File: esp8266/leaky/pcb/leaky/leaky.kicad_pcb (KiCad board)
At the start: 2 copper layers, 100 x 100 mm, 31 parts, among them J1 UART, J2 extra pins, Q1 BC327, SW1 sensing loop, U1 DD0405MA, U2 ESP-12F

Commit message: leaky: Add more traces
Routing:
- net Net-(R1-Pad2): track 2411.8 -> 2436.5 mm
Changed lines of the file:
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@@
   (general
     (thickness 1.6)
-    (drawings 34)
-    (tracks 342)
+    (drawings 33)
+    (tracks 351)
     (zones 0)
     (modules 31)
@@
   )
   (setup
-    (last_trace_width 0.5)
+    (last_trace_width 0.25)
     (user_trace_width 0.4)
     (user_trace_width 0.5)
@@
     (mod_text_size 1 1)
     (mod_text_width 0.15)
-    (pad_size 1.524 1.524)
-    (pad_drill 0.762)
+    (pad_size 3.2 3.2)
+    (pad_drill 3.2)
     (pad_to_mask_clearance 0)
     (aux_axis_origin 0 0)
@@
       (effects (font (size 1 1) (thickness 0.15)))
     )
-    (pad 1 np_thru_hole circle (at 0 0) (size 3.2 3.2) (drill 3.2) (layers *.Cu *.Mask))
+    (pad "" np_thru_hole circle (at 0 0) (size 3.2 3.2) (drill 3.2) (layers *.Cu *.Mask)
+      (clearance 2))
   )
   (module _my:MountingHole_3.2mm_M3 (layer F.Cu)
@@
       (effects (font (size 1 1) (thickness 0.15)))
     )
-    (pad 1 np_thru_hole circle (at 0 0) (size 3.2 3.2) (drill 3.2) (layers *.Cu *.Mask))
+    (pad "" np_thru_hole circle (at 0 0) (size 3.2 3.2) (drill 3.2) (layers *.Cu *.Mask)
+      (clearance 2))
   )
   (module _my:CP_Radial_D10.0mm_P5.00mm (layer F.Cu)
@@
   (gr_arc (start 25 115) (end 20 115) (angle -90) (layer Edge.Cuts) (width 0.05))
   (gr_arc (start 71 120) (end 72 120) (angle -180) (layer Edge.Cuts) (width 0.05))
-  (gr_poly (pts (xy 119.2 111.2) (xy 110.9 111.2) (xy 110.9 28.8) (xy 119.2 28.8)) (layer F.Mask) (width 0.1))
   (gr_text "RXD->TX\nTXD->RX" (at 25 73.2 270) (layer F.SilkS)
     (effects (font (size 1 1) (thickness 0.15)) (justify left))
@@
     (effects (font (size 1 1) (thickness 0.15)) (justify right))
   )
-  (gr_poly (pts (xy 111.2 119.5) (xy 71 119.5) (xy 71 20.5) (xy 111.2 20.5)) (layer F.Mask) (width 0.1))
+  (gr_poly (pts (xy 119.7 119.5) (xy 71 119.5) (xy 71 20.5) (xy 119.7 20.5)) (layer F.Mask) (width 0.1))
   (gr_line (start 20 115) (end 20 25) (layer Edge.Cuts) (width 0.05))
   (gr_line (start 120 25) (end 120 115) (layer Edge.Cuts) (width 0.05))
+  (segment (start 119 110) (end 119 115) (width 0.5) (layer F.Cu) (net 20))
+  (segment (start 119 25.1) (end 119 28.7) (width 0.5) (layer F.Cu) (net 20))
+  (segment (start 119 26.4) (end 119 30) (width 0.5) (layer F.Cu) (net 20))
   (segment (start 67.84 85.72) (end 67.84 88.16) (width 1) (layer F.Cu) (net 1))
   (segment (start 67.84 88.16) (end 62.75 93.25) (width 1) (layer F.Cu) (net 1))
@@
   (segment (start 110.5 24) (end 72 24) (width 1) (layer F.Cu) (net 20))
   (segment (start 72 22.1) (end 72 110) (width 1) (layer F.Cu) (net 20))
-  (segment (start 72 22.1) (end 72 21.75) (width 0.5) (layer F.Cu) (net 20))
-  (segment (start 72 21.75) (end 72.75 21) (width 0.5) (layer F.Cu) (net 20))
-  (segment (start 72.75 21) (end 99.75 21) (width 0.5) (layer F.Cu) (net 20))
-  (segment (start 99.75 21) (end 110.75 21) (width 0.5) (layer F.Cu) (net 20))
   (segment (start 99.7 119) (end 110.7 119) (width 0.5) (layer F.Cu) (net 20))
   (segment (start 72.65 119) (end 99.65 119) (width 0.5) (layer F.Cu) (net 20))
   (segment (start 72 118.35) (end 72.65 119) (width 0.5) (layer F.Cu) (net 20))
   (segment (start 72 117.9) (end 72 118.35) (width 0.5) (layer F.Cu) (net 20))
+  (segment (start 110.75 21) (end 115 21) (width 0.5) (layer F.Cu) (net 20))
+  (segment (start 72.75 21) (end 110.75 21) (width 0.5) (layer F.Cu) (net 20))
+  (segment (start 72 21.75) (end 72.75 21) (width 0.5) (layer F.Cu) (net 20))
+  (segment (start 72 22.1) (end 72 21.75) (width 0.5) (layer F.Cu) (net 20))
+  (segment (start 110.7 119) (end 111.25 119) (width 0.5) (layer F.Cu) (net 20))
+  (segment (start 111.25 119) (end 115 119) (width 0.5) (layer F.Cu) (net 20))
+  (segment (start 110.5 112) (end 111.5 112) (width 1) (layer F.Cu) (net 20))
+  (segment (start 110.5 117.9) (end 111.5 117.9) (width 1) (layer F.Cu) (net 20))
+  (segment (start 110.5 28) (end 111.5 28) (width 1) (layer F.Cu) (net 20))
+  (segment (start 110.5 22.1) (end 111.5 22.1) (width 1) (layer F.Cu) (net 20))
   (zone (net 2) (net_name GND) (layer B.Cu) (hatch edge 0.508)
     (connect_pads (clearance 0.508))

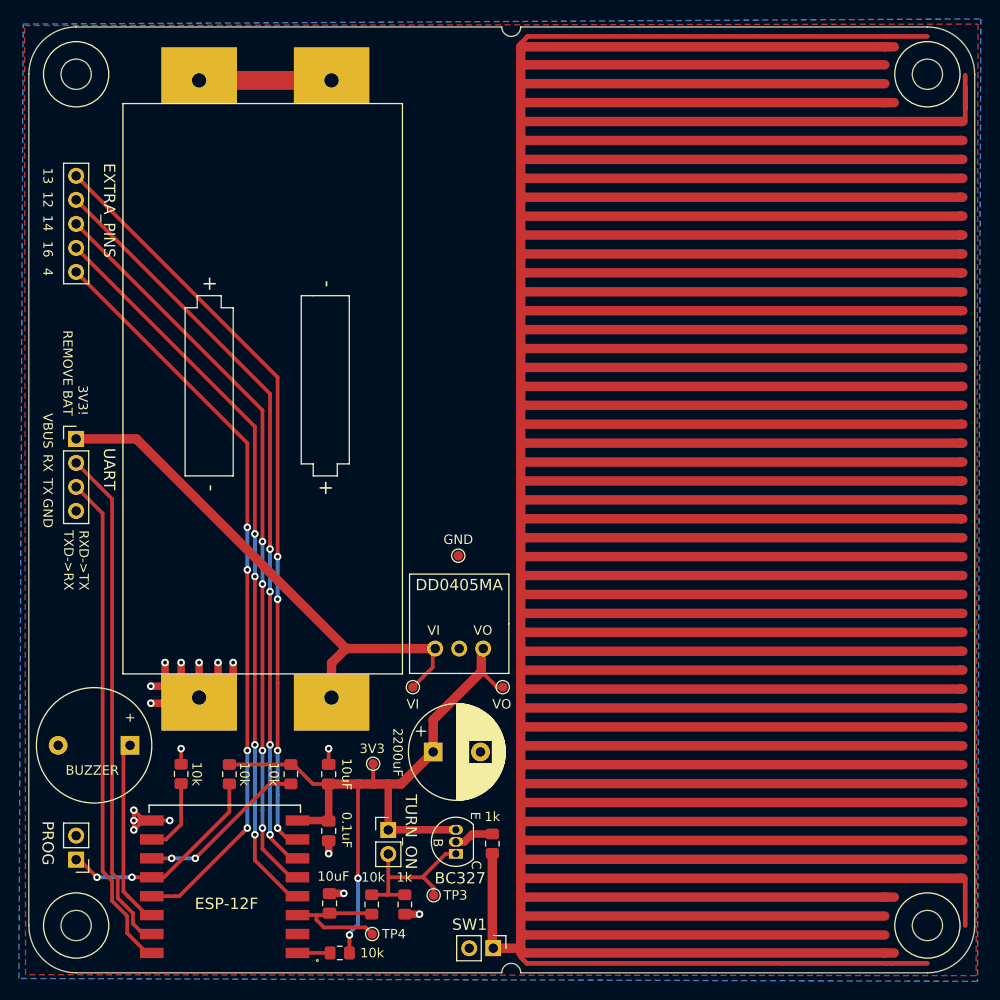
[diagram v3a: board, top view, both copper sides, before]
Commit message: leaky: Remove solder mask
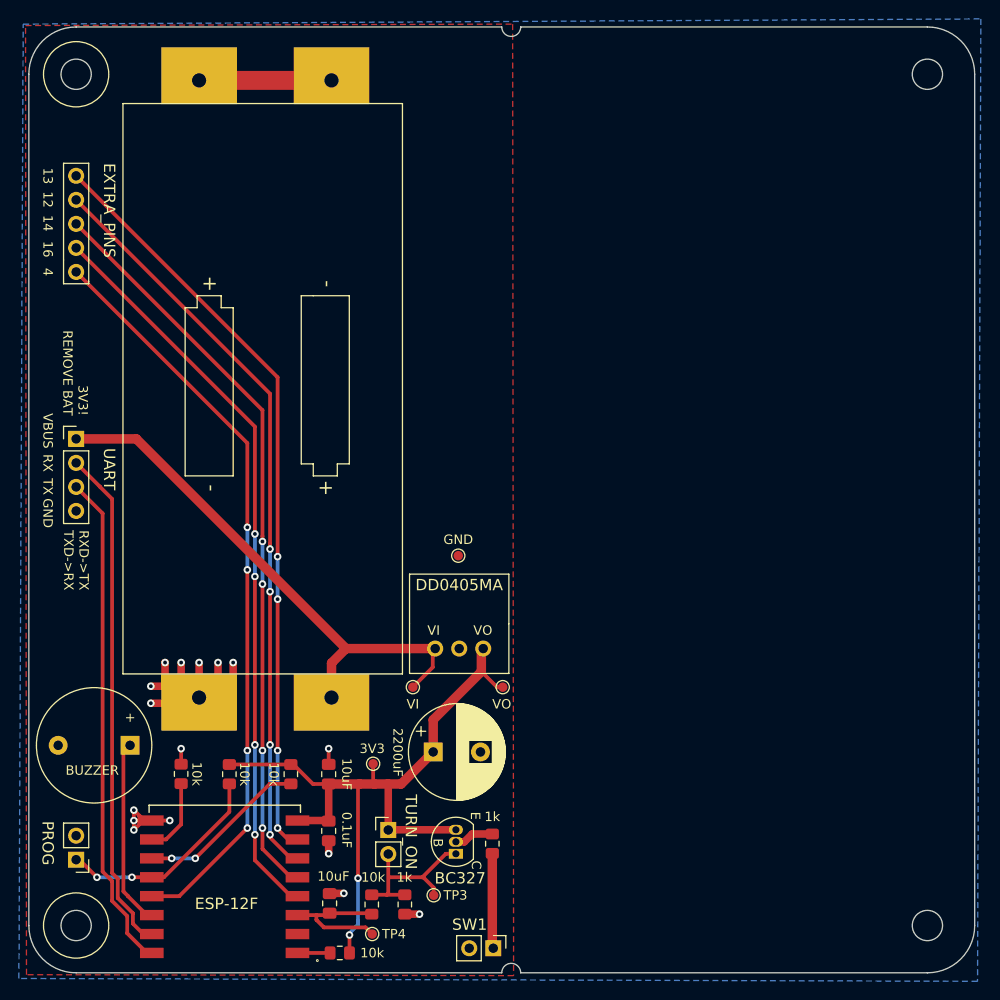
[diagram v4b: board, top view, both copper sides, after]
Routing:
- net Net-(R1-Pad2): track 2436.5 -> 10.1 mm

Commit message: leaky: Top sensing is done
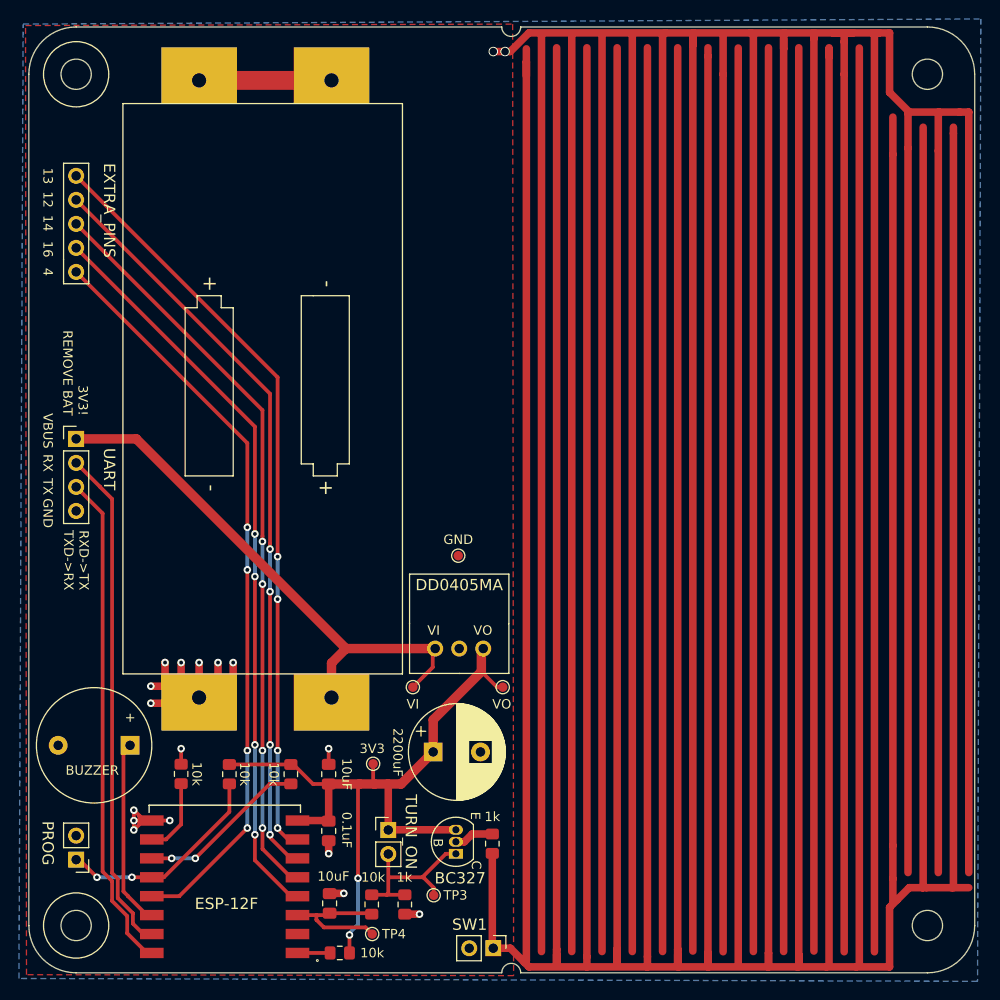
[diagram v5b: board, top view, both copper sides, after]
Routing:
- net Net-(R1-Pad2): track 10.1 -> 1490.2 mm
- net GND: track 54.5 -> 1522.5 mm, vias 16 -> 18
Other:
- net class Sensing: clearance 0.5 -> 0.2; trace_width 1 -> 0.8

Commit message: leaky: Try upload gerbs
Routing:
- net GND: track 1522.5 -> 1524.2 mm
